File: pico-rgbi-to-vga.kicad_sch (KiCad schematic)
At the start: 28 parts, among them J1 SDS-80J, J2 DB15_Female_HighDensity, J3 USB-B1HSB6, Q1 2n2222, Q2 2n2222, U1 Pico

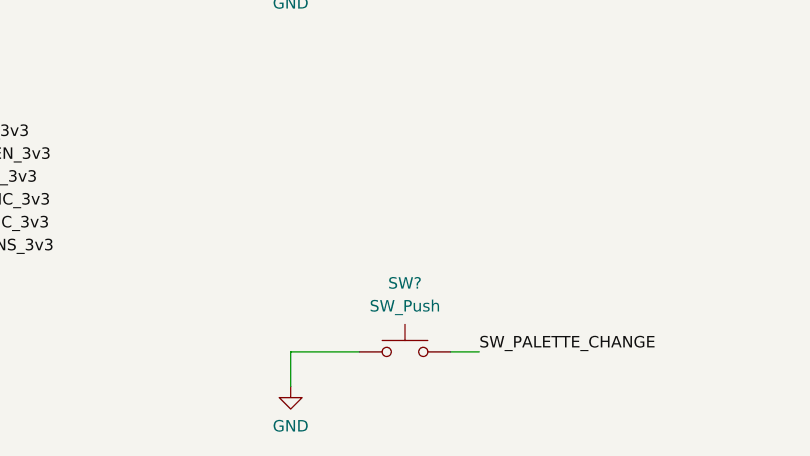
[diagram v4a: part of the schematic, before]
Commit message: Palette toggle button
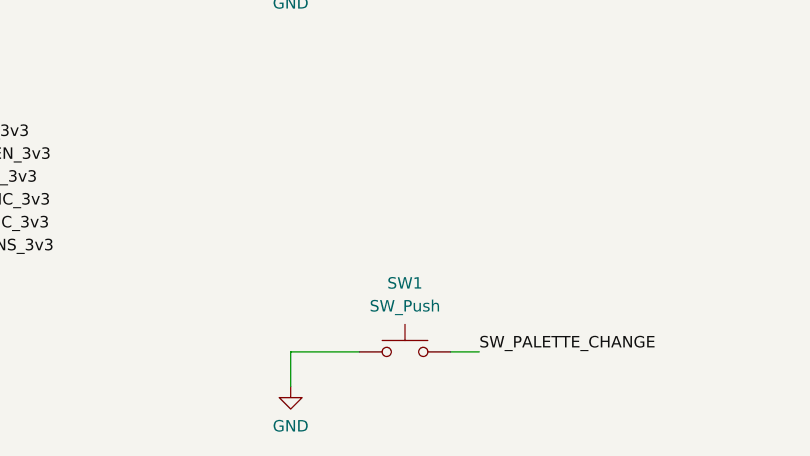
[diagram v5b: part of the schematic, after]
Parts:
- gave numbers to parts that had none: 1
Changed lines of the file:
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@@
   (symbol (lib_id "power:GND") (at 120.65 158.115 0) (unit 1)
     (in_bom yes) (on_board yes) (fields_autoplaced)
-    (property "Reference" "#PWR?" (id 0) (at 120.65 164.465 0)
+    (property "Reference" "#PWR0116" (id 0) (at 120.65 164.465 0)
       (effects (font (size 1.27 1.27)) hide)
     )
@@
   (symbol (lib_id "Switch:SW_Push") (at 133.35 154.305 0) (unit 1)
     (in_bom yes) (on_board yes) (fields_autoplaced)
-    (property "Reference" "SW?" (id 0) (at 133.35 146.685 0))
+    (property "Reference" "SW1" (id 0) (at 133.35 146.685 0))
     (property "Value" "SW_Push" (id 1) (at 133.35 149.225 0))
     (property "Footprint" "Button_Switch_THT:SW_PUSH_6mm" (id 2) (at 133.35 149.225 0)
@@
     )
     (path "/299a2b70-4a8f-4ddd-803b-9f2688cbf498"
-      (reference "#PWR?") (unit 1) (value "GND") (footprint "")
+      (reference "#PWR0116") (unit 1) (value "GND") (footprint "")
     )
     (path "/e74ce1bf-af97-407b-b11d-d350e934d692"
@@
     )
     (path "/3ebb7414-8370-4606-bcb1-2b26f5893364"
-      (reference "SW?") (unit 1) (value "SW_Push") (footprint "Button_Switch_THT:SW_PUSH_6mm")
+      (reference "SW1") (unit 1) (value "SW_Push") (footprint "Button_Switch_THT:SW_PUSH_6mm")
     )
     (path "/2674e903-9fe3-4a69-b6af-9ed5ebc97bf1"

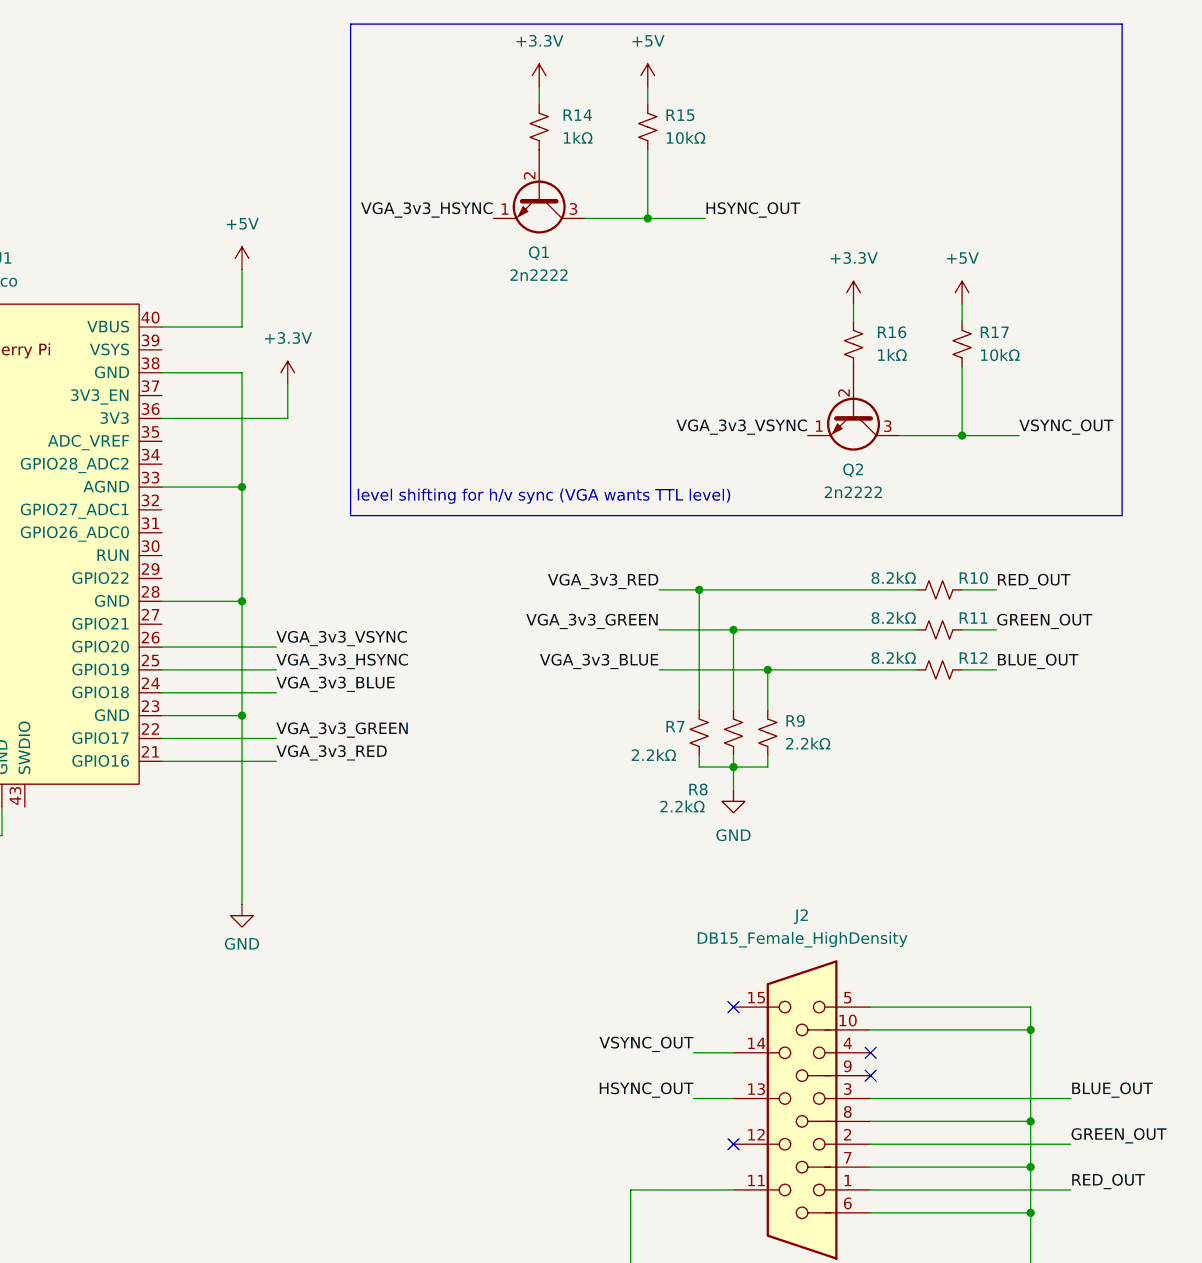
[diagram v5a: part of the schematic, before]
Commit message: Use PicoVGA resistor ladder
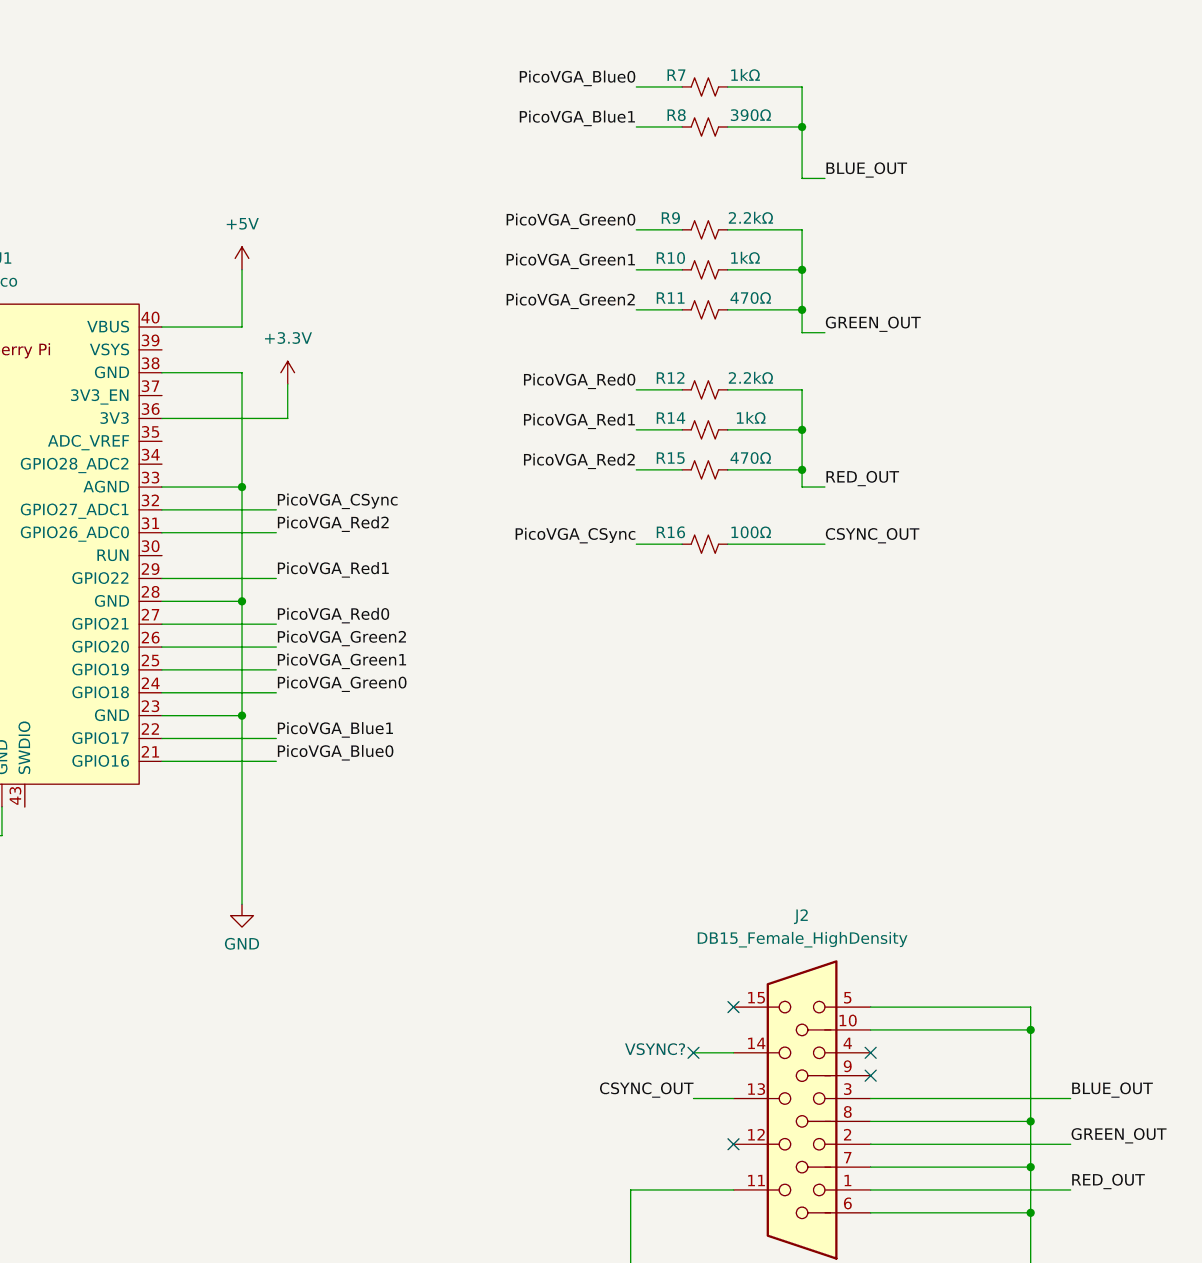
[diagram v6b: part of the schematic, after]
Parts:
- removed Q1, Q2: 2n2222, Package_TO_SOT_THT:TO-92_Inline, symbol Device:Q_NPN_EBC
- removed R17: 10kΩ, Resistor_SMD:R_0805_2012Metric_Pad1.20x1.40mm_HandSolder, symbol Device:R_Small_US
- R10: value 8.2kΩ -> 1kΩ
- R11: value 8.2kΩ -> 470Ω
- R12: value 8.2kΩ -> 2.2kΩ
- R15: value 10kΩ -> 470Ω
- R16: value 1kΩ -> 100Ω
- R7: value 2.2kΩ -> 1kΩ
- R8: value 2.2kΩ -> 390Ω
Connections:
- net +3V3: no longer R14.1, R16.1
- net +5V: no longer R15.1
- net BLUE_OUT: now also R7.2, R8.2; no longer R12.2
- net GND: no longer R7.2, R8.2, R9.2
- net GREEN_OUT: now also R10.2, R9.2
- net RED_OUT: now also R12.2, R14.2, R15.2; no longer R10.2
- net PicoVGA_Red0: now reaches U1.27 (GPIO21)
- net PicoVGA_Red0: now also R12.1
- net PicoVGA_Red1: now reaches U1.29 (GPIO22)
- net PicoVGA_Red1: now also R14.1
- net PicoVGA_Red2: now reaches U1.31 (GPIO26_ADC0)
- net PicoVGA_Red2: now also R15.1
- net PicoVGA_CSync: now reaches U1.32 (GPIO27_ADC1)
- net PicoVGA_CSync: now also R16.1
- net CSYNC_OUT: now reaches R16.2
- net CSYNC_OUT: now also J2.13
- removed net HSYNC_OUT: J2.13, R15.2
- net VGA_3v3_BLUE renamed PicoVGA_Green0
- net PicoVGA_Green0: no longer R12.1
- net VGA_3v3_GREEN renamed PicoVGA_Blue1
- net PicoVGA_Blue1: no longer R11.1
- net VGA_3v3_HSYNC renamed PicoVGA_Green1
- net PicoVGA_Green1: now also R10.1
- net VGA_3v3_RED renamed PicoVGA_Blue0
- net PicoVGA_Blue0: no longer R10.1
- net VGA_3v3_VSYNC renamed PicoVGA_Green2
- net PicoVGA_Green2: now also R11.1
- net VSYNC_OUT: no longer names the net of J2.14
- no-connect marks 6 -> 7
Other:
- note added: "VSYNC?"
- note removed: "level shifting for h/v sync (VGA wants TTL level)"

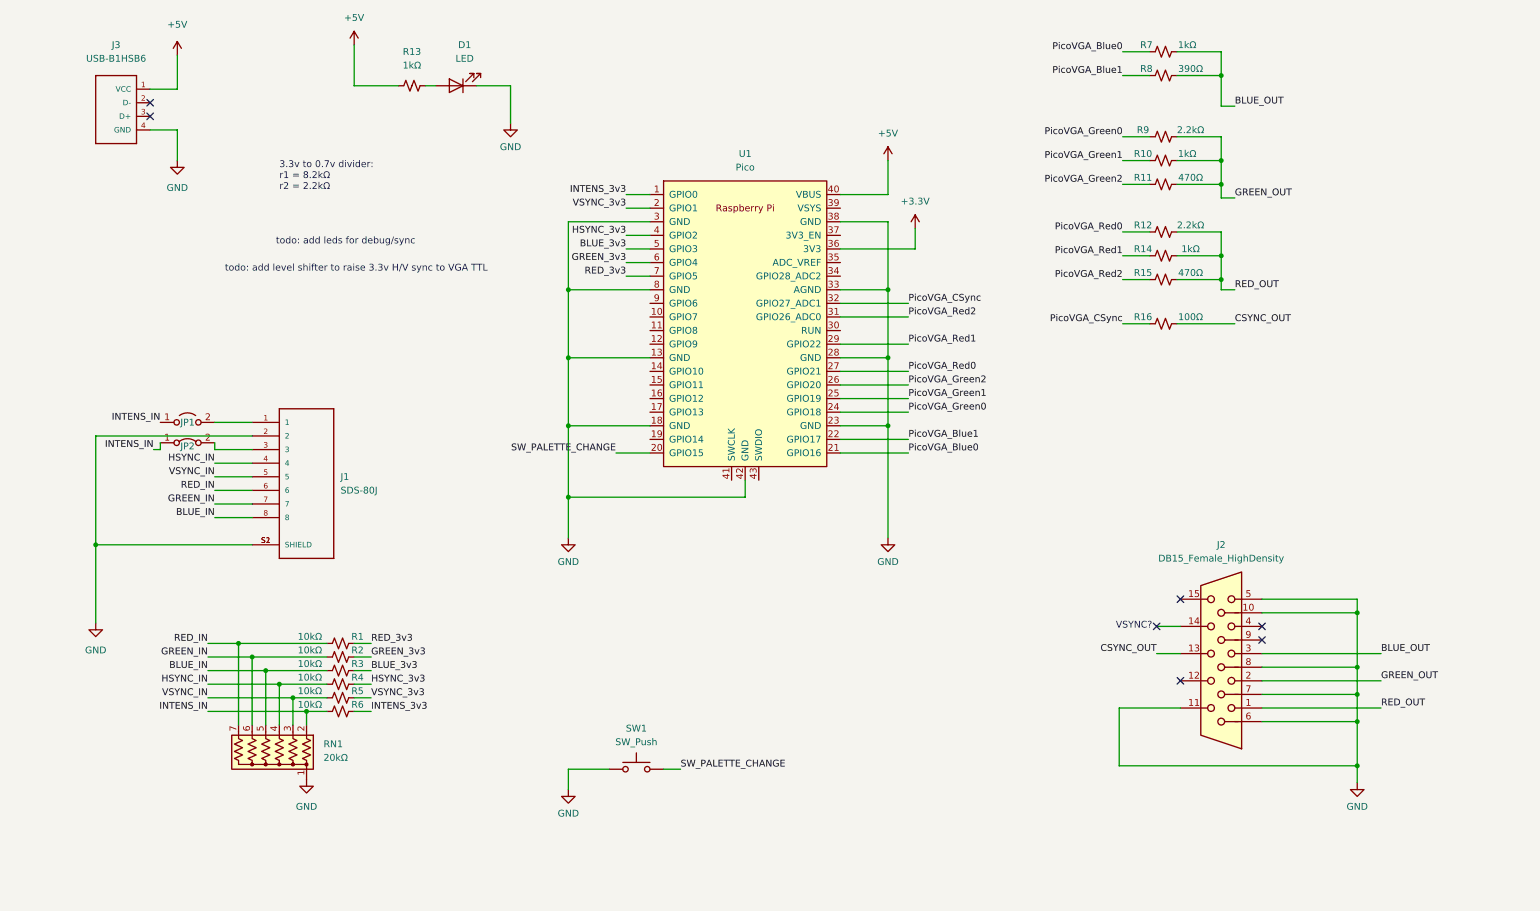
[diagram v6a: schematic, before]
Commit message: Change divider values
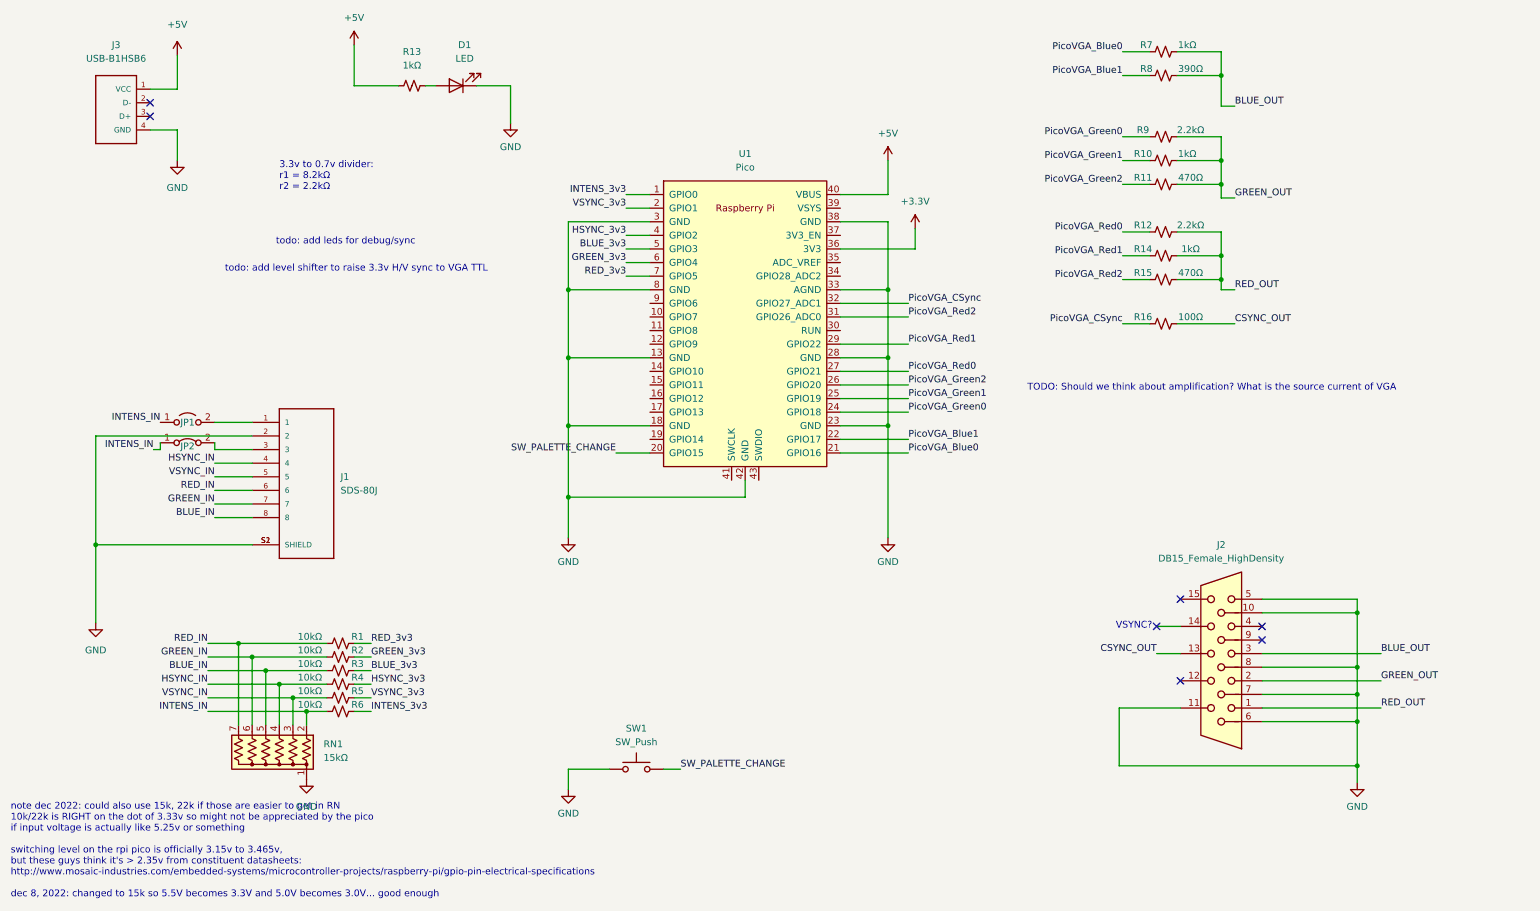
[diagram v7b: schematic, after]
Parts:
- RN1: value 20kΩ -> 15kΩ; Mouser (none) -> 652-4607X-1LF-22K
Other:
- note added: "TODO: Should we think about amplification? What is the source current of VGA"
- note added: "note dec 2022: could also use 15k, 22k if those are easier to get in RN 10k/22k is RIGHT on the dot of 3.33v so might not be appreciated by the pico if input voltage is actually like 5.25v or something switching level on the rpi pico is officially 3.15v to 3.465v, but these guys think it's > 2.35v from constituent datasheets: http://www.mosaic-industries.com/embedded-systems/microcontroller-proje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"
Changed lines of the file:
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@@
     (stroke (width 0) (type default) (color 0 0 0 0))
   )
+  (text "TODO: Should we think about amplification? What is the source current of VGA"
+    (at 206.375 83.82 0)
+    (effects (font (size 1.27 1.27)) (justify left bottom))
+  )
   (text "3.3v to 0.7v divider:\nr1 = 8.2kΩ\nr2 = 2.2kΩ" (at 66.675 46.355 0)
     (effects (font (size 1.27 1.27)) (justify left bottom))
@@
   )
   (text "VSYNC?" (at 222.885 128.27 0)
+    (effects (font (size 1.27 1.27)) (justify left bottom))
+  )
+  (text "note dec 2022: could also use 15k, 22k if those are easier to get in RN\n10k/22k is RIGHT on the dot of 3.33v so might not be appreciated by the pico\nif input voltage is actually like 5.25v or something\n\nswitching level on the rpi pico is officially 3.15v to 3.465v,\nbut these guys think it's > 2.35v from constituent datasheets:\nhttp://www.mosaic-industries.com/embedded-systems/microcontroller-projects/raspberry-pi/gpio-pin-electrical-specifications\n\ndec 8, 2022: changed to 15k so 5.5V becomes 3.3V and 5.0V becomes 3.0V... good enough"
+    (at 16.51 178.435 0)
     (effects (font (size 1.27 1.27)) (justify left bottom))
   )
@@
       (effects (font (size 1.27 1.27)) (justify right))
     )
-    (property "Value" "20kΩ" (id 1) (at 74.93 152.1459 0)
+    (property "Value" "15kΩ" (id 1) (at 74.93 152.1459 0)
       (effects (font (size 1.27 1.27)) (justify right))
     )
@@
     )
     (property "Datasheet" "http://www.vishay.com/docs/31509/csc.pdf" (id 3) (at 64.135 151.13 0)
+      (effects (font (size 1.27 1.27)) hide)
+    )
+    (property "Mouser" "652-4607X-1LF-22K" (id 5) (at 64.135 151.13 0)
       (effects (font (size 1.27 1.27)) hide)
     )
@@
     )
     (path "/dcda6a74-0460-40e6-8ee3-a792f5780acc"
-      (reference "RN1") (unit 1) (value "20kΩ") (footprint "Resistor_THT:R_Array_SIP7")
+      (reference "RN1") (unit 1) (value "15kΩ") (footprint "Resistor_THT:R_Array_SIP7")
     )
     (path "/3ebb7414-8370-4606-bcb1-2b26f5893364"
